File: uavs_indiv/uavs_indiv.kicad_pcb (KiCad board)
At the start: 2 copper layers, 105 x 56 mm, 17 parts, among them J1 Conn_01x02_Socket, J2 Conn_01x04_Pin, J3 Conn_01x04_Pin, J6 Conn_01x04_Pin, U1 LM2576HVS-5, U3 LM2576HVS-5

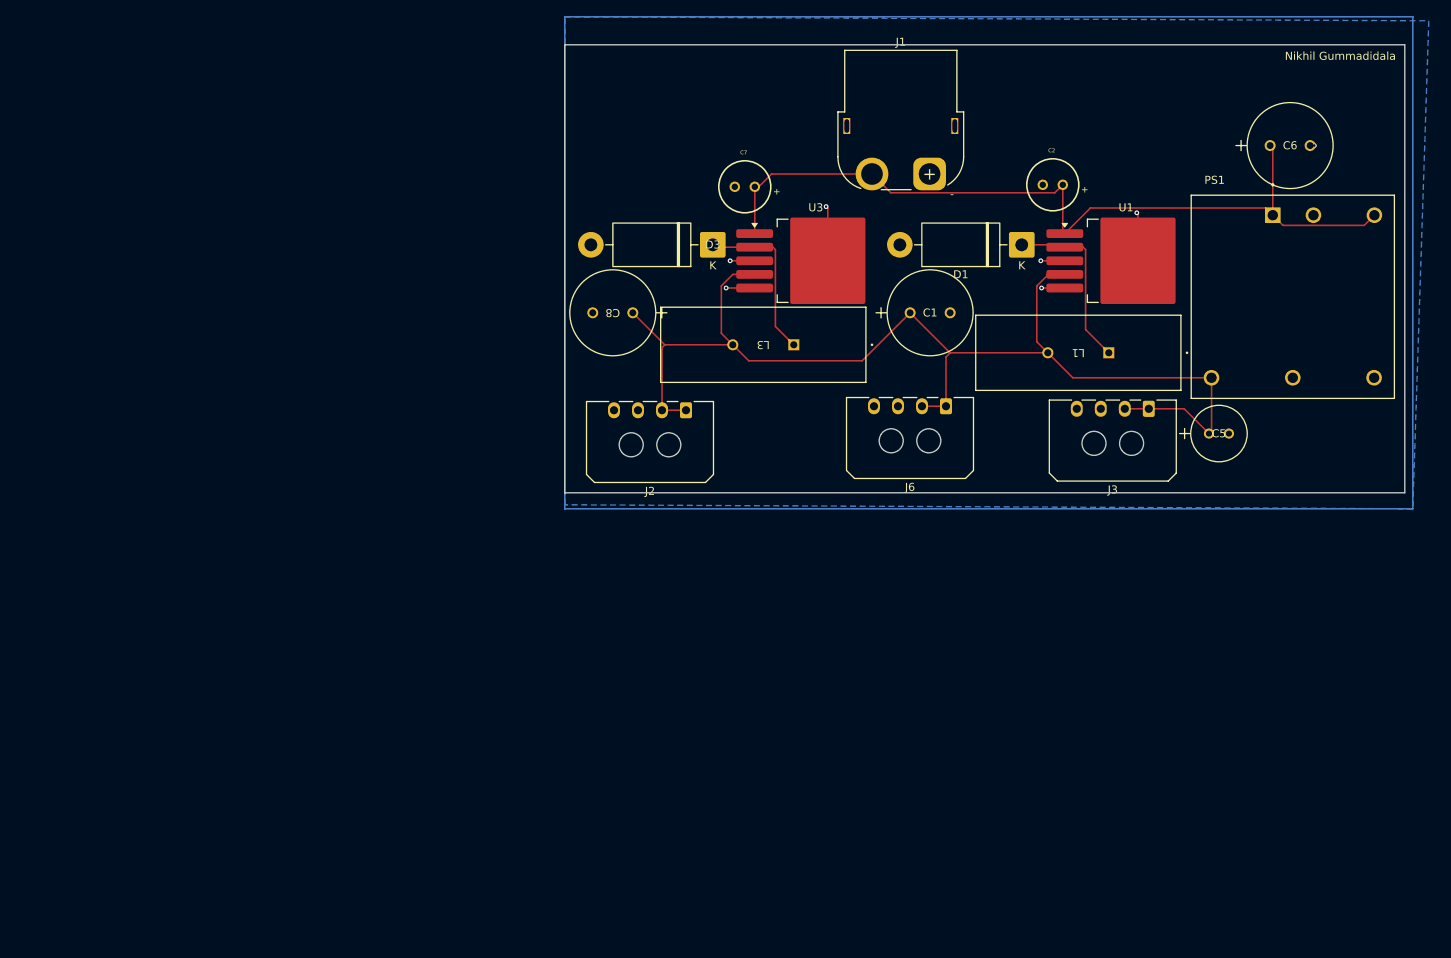
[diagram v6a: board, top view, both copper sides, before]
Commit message: made traces bigger added space between components added screw holes added one more 5v output (unisolated)
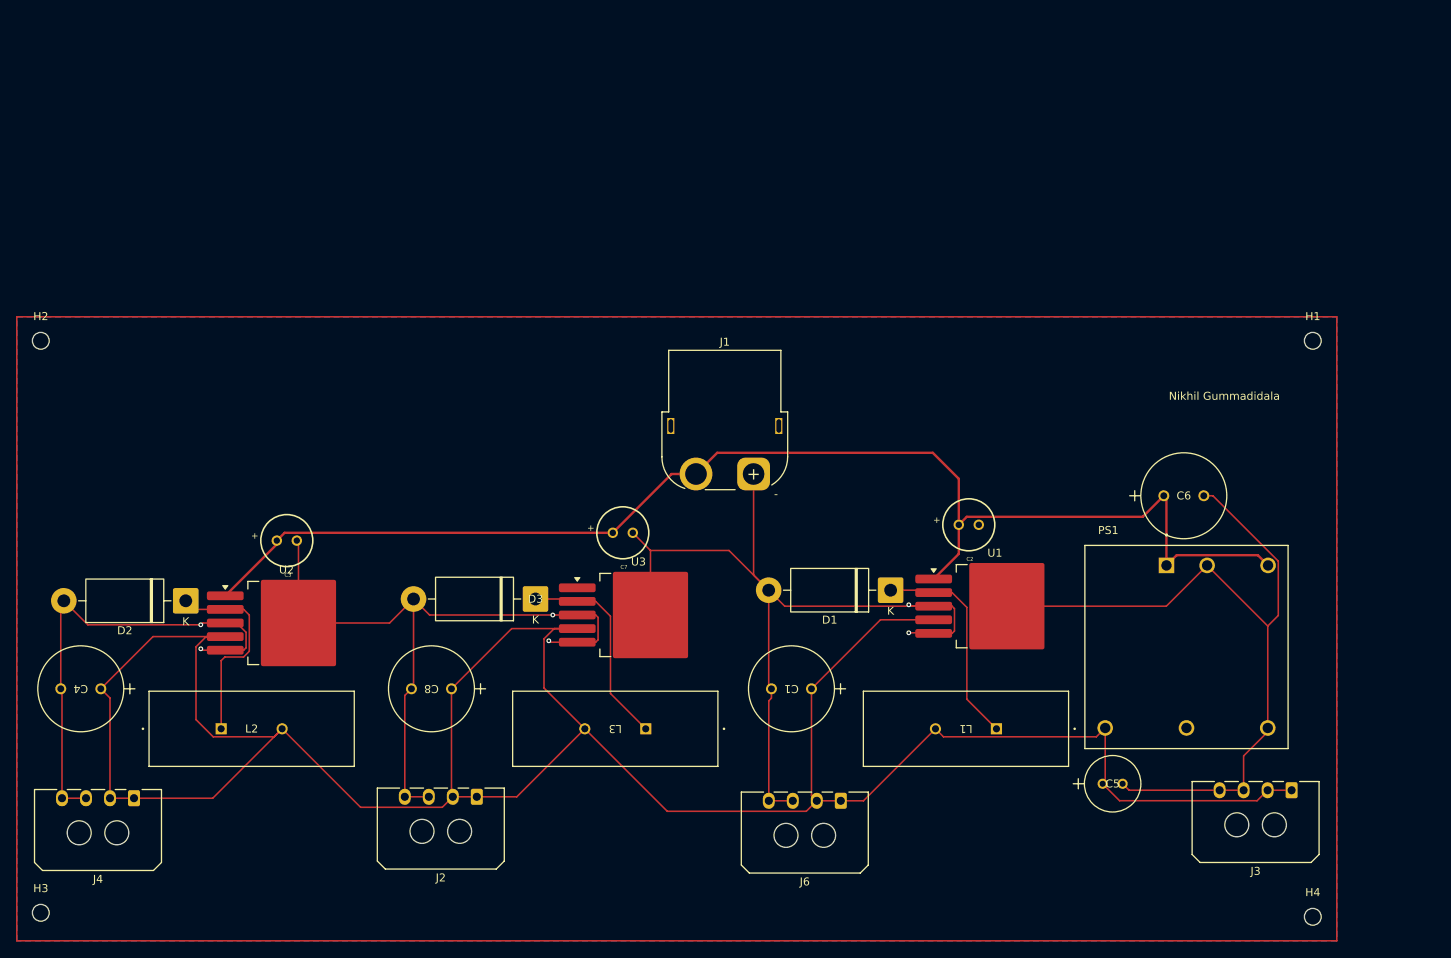
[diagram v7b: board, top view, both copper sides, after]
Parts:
- added C3: 100uF, customdcdc:capacitor100uf, F.Cu at (94.2, 88.0)
- added C4: 1000uF, customdcdc:capacitor1000uf, F.Cu at (71.0, 106.5)
- added D2: 1N5822, Diode_THT:D_DO-201AD_P15.24mm_Horizontal, F.Cu at (81.6, 95.5)
- added H1: MountingHole, MountingHole:MountingHole_2.1mm, F.Cu at (222.5, 63.0)
- added H2: MountingHole, MountingHole:MountingHole_2.1mm, F.Cu at (63.5, 63.0)
- added H3: MountingHole, MountingHole:MountingHole_2.1mm, F.Cu at (63.5, 134.5)
- added H4: MountingHole, MountingHole:MountingHole_2.1mm, F.Cu at (222.5, 135.0)
- added J4: Conn_01x04_Pin, customdcdc:Molex_Micro-Fit_3.0_43650-0400_1x04_P3.00mm_Horizontal, F.Cu at (75.2, 120.2)
- added L2: 100u, customdcdc:inductor3.5a100u, F.Cu at (86.0, 111.5)
- added U2: LM2576HVS-5, Package_TO_SOT_SMD:TO-263-5_TabPin3, F.Cu at (94.2, 98.3)
- moved J2 54.9 mm to (118.0, 120.0)
- moved C8 52.2 mm to (114.8, 106.5)
- moved L3 51.4 mm to (139.1, 111.5)
- moved J6 51.0 mm to (163.5, 120.5)
- moved J3 50.9 mm to (219.8, 119.2)
- moved U3 49.5 mm to (138.2, 97.3)
- moved D3 49.5 mm to (125.3, 95.3)
- moved L1 49.1 mm to (183.0, 111.5)
- moved C1 48.6 mm to (159.8, 106.5), turned to 180 degrees
- moved D1 46.2 mm to (169.7, 94.2)
- moved U1 46.2 mm to (182.8, 96.2)
- moved C7 45.9 mm to (136.2, 87.0), turned to 180 degrees
- moved C5 45.7 mm to (196.2, 118.4)
- moved C6 45.7 mm to (203.9, 82.4)
- moved PS1 45.7 mm to (206.7, 101.3)
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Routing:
- net GND: track 25.4 -> 354.1 mm, vias 10 -> 28
- net +5V: track 149.7 -> 320.5 mm
- net /Vin: track 104.4 -> 164.3 mm
- net Net-(D2-K): track 0.00 -> 25.7 mm
- net Net-(D1-K): track 21.8 -> 27.1 mm
- net Net-(D3-K): track 20.9 -> 26.2 mm
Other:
- board outline removed

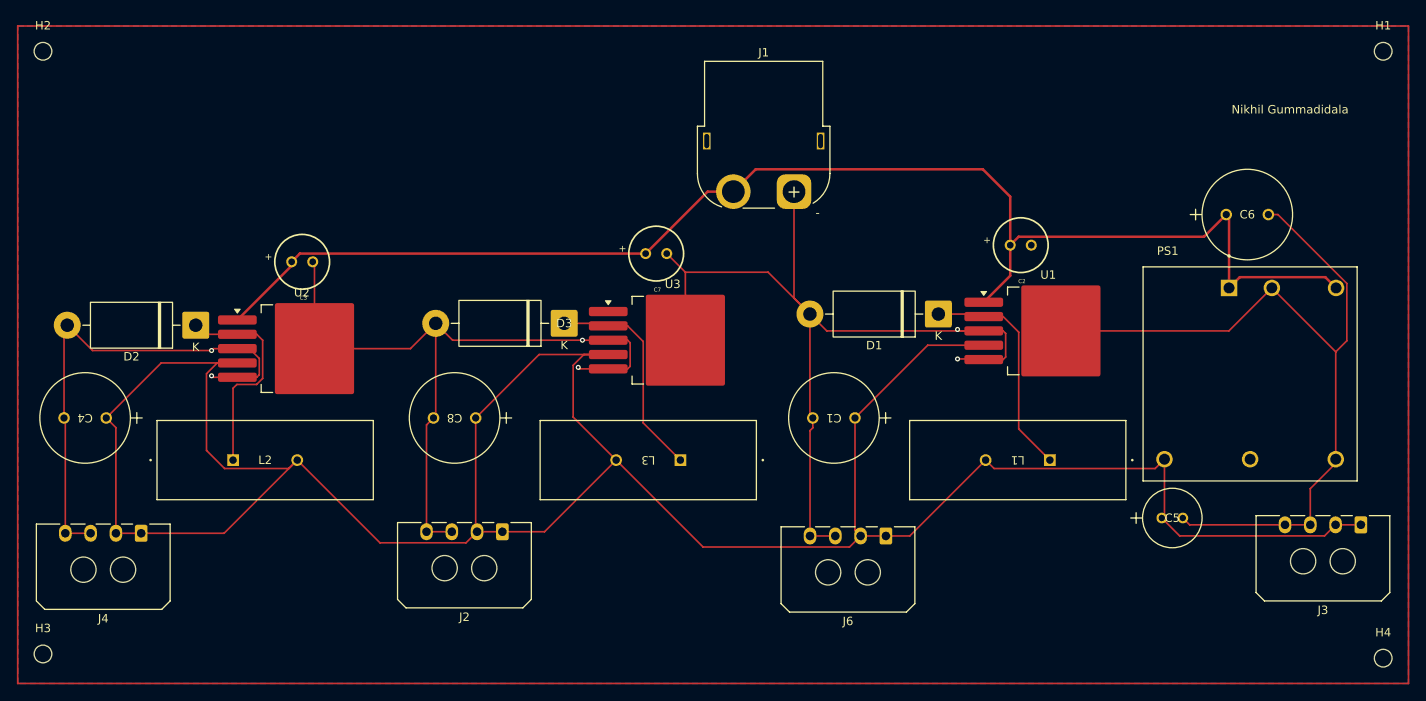
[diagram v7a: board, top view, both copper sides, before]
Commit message: added filled copper zone for vin
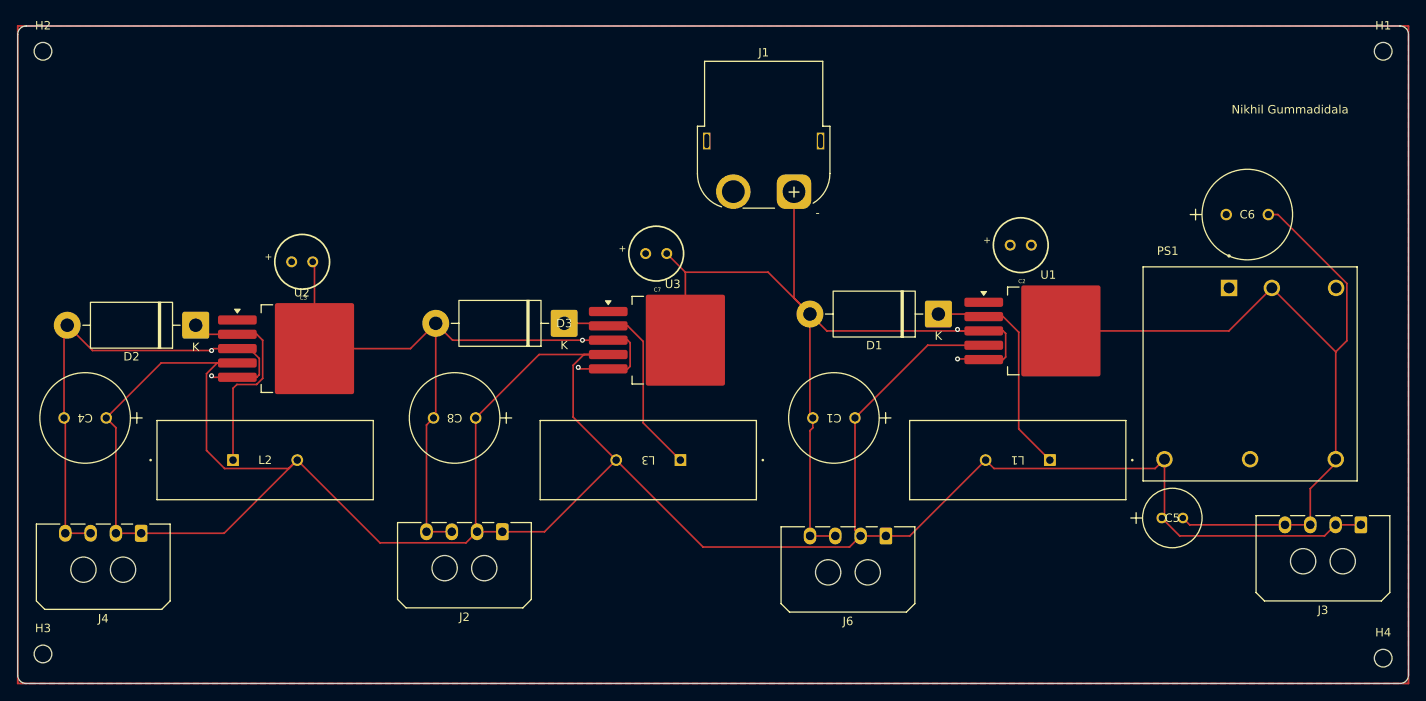
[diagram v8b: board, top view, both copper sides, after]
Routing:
- net /Vin: track 164.3 -> 0.93 mm
- added copper zone on F.Cu, net /Vin
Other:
- board outline added: 165 x 78 mm
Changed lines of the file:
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@@
 		(layer "F.Cu")
+	)
+	(gr_line
+		(start 60.5 137)
+		(end 60.5 61)
+		(stroke
+			(width 0.05)
+			(type default)
+		)
+		(layer "Edge.Cuts")
+	)
+	(gr_line
+		(start 61.5 60)
+		(end 224.5 60)
+		(stroke
+			(width 0.05)
+			(type default)
+		)
+		(layer "Edge.Cuts")
+	)
+	(gr_arc
+		(start 225.5 137)
+		(mid 225.207107 137.707107)
+		(end 224.5 138)
+		(stroke
+			(width 0.05)
+			(type default)
+		)
+		(layer "Edge.Cuts")
+	)
+	(gr_line
+		(start 225.5 61)
+		(end 225.5 137)
+		(stroke
+			(width 0.05)
+			(type default)
+		)
+		(layer "Edge.Cuts")
+	)
+	(gr_arc
+		(start 60.5 61)
+		(mid 60.792893 60.292893)
+		(end 61.5 60)
+		(stroke
+			(width 0.05)
+			(type default)
+		)
+		(layer "Edge.Cuts")
+	)
+	(gr_line
+		(start 224.5 138)
+		(end 61.5 138)
+		(stroke
+			(width 0.05)
+			(type default)
+		)
+		(layer "Edge.Cuts")
+	)
+	(gr_arc
+		(start 224.5 60)
+		(mid 225.207107 60.292893)
+		(end 225.5 61)
+		(stroke
+			(width 0.05)
+			(type default)
+		)
+		(layer "Edge.Cuts")
+	)
+	(gr_arc
+		(start 61.5 138)
+		(mid 60.792893 137.707107)
+		(end 60.5 137)
+		(stroke
+			(width 0.05)
+			(type default)
+		)
+		(layer "Edge.Cuts")
 	)
 	(gr_text "Nikhil Gummadidala"
@@
 	)
 	(segment
-		(start 201.2466 85)
-		(end 203.8766 82.37)
-		(width 0.3)
-		(layer "F.Cu")
-		(net 3)
-	)
-	(segment
 		(start 93 88.43485)
 		(end 93 87.975)
@@
 	)
 	(segment
-		(start 178.25 89.63285)
-		(end 175.10885 92.774)
-		(width 0.3)
-		(layer "F.Cu")
-		(net 3)
-	)
-	(segment
-		(start 142.35 79.65)
-		(end 145.4 79.65)
-		(width 0.3)
-		(layer "F.Cu")
-		(net 3)
-	)
-	(segment
-		(start 135 87)
-		(end 142.35 79.65)
-		(width 0.3)
-		(layer "F.Cu")
-		(net 3)
-	)
-	(segment
-		(start 86.55985 94.875)
-		(end 93 88.43485)
-		(width 0.3)
-		(layer "F.Cu")
-		(net 3)
-	)
-	(segment
-		(start 145.4 79.65)
-		(end 148.05 77)
-		(width 0.3)
-		(layer "F.Cu")
-		(net 3)
-	)
-	(segment
-		(start 178.25 80.25)
-		(end 178.25 86)
-		(width 0.3)
-		(layer "F.Cu")
-		(net 3)
-	)
-	(segment
-		(start 93.975 87)
-		(end 135 87)
-		(width 0.3)
-		(layer "F.Cu")
-		(net 3)
-	)
-	(segment
-		(start 178.25 86)
-		(end 178.25 89.63285)
-		(width 0.3)
-		(layer "F.Cu")
-		(net 3)
-	)
-	(segment
-		(start 205.48585 89.799)
-		(end 215.63385 89.799)
-		(width 0.3)
-		(layer "F.Cu")
-		(net 3)
-	)
-	(segment
-		(start 215.63385 89.799)
-		(end 216.90985 91.075)
-		(width 0.3)
-		(layer "F.Cu")
-		(net 3)
-	)
-	(segment
 		(start 204.20985 82.70325)
 		(end 203.8766 82.37)
@@
 	)
 	(segment
-		(start 179.25 85)
-		(end 201.2466 85)
-		(width 0.3)
-		(layer "F.Cu")
-		(net 3)
-	)
-	(segment
-		(start 204.20985 91.075)
-		(end 204.20985 82.70325)
-		(width 0.3)
-		(layer "F.Cu")
-		(net 3)
-	)
-	(segment
-		(start 204.20985 91.075)
-		(end 205.48585 89.799)
-		(width 0.3)
-		(layer "F.Cu")
-		(net 3)
-	)
-	(segment
-		(start 175 77)
-		(end 178.25 80.25)
-		(width 0.3)
-		(layer "F.Cu")
-		(net 3)
-	)
-	(segment
-		(start 178.25 86)
-		(end 179.25 85)
-		(width 0.3)
-		(layer "F.Cu")
-		(net 3)
-	)
-	(segment
-		(start 148.05 77)
-		(end 175 77)
-		(width 0.3)
-		(layer "F.Cu")
-		(net 3)
-	)
-	(segment
-		(start 93 87.975)
-		(end 93.975 87)
-		(width 0.3)
-		(layer "F.Cu")
-		(net 3)
-	)
-	(segment
 		(start 177.40885 94.474)
 		(end 175.10885 94.474)
@@
 	)
 	(zone
+		(net 3)
+		(net_name "/Vin")
+		(layer "F.Cu")
+		(hatch edge 0.5)
+		(priority 1)
+		(connect_pads
+			(clearance 0.5)
+		)
+		(min_thickness 0.25)
+		(filled_areas_thickness no)
+		(fill yes
+			(thermal_gap 0.5)
+			(thermal_bridge_width 0.5)
+		)
+		(polygon
+			(pts
+				(xy 60.5 60) (xy 225.5 60) (xy 225.5 138) (xy 60.5 138)
+			)
+		)
+	)
+	(zone
